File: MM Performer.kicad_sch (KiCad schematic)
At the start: 39 parts, among them IC1 MC68000P, U1 MC68030RC, U2 MC68881FN-SOC, U3 ATF16V8BJ, U4 ATF16V8BJ, U5 ATF16V8BJ, U6 ATF16V8BJ, U7 ATF16V8BJ

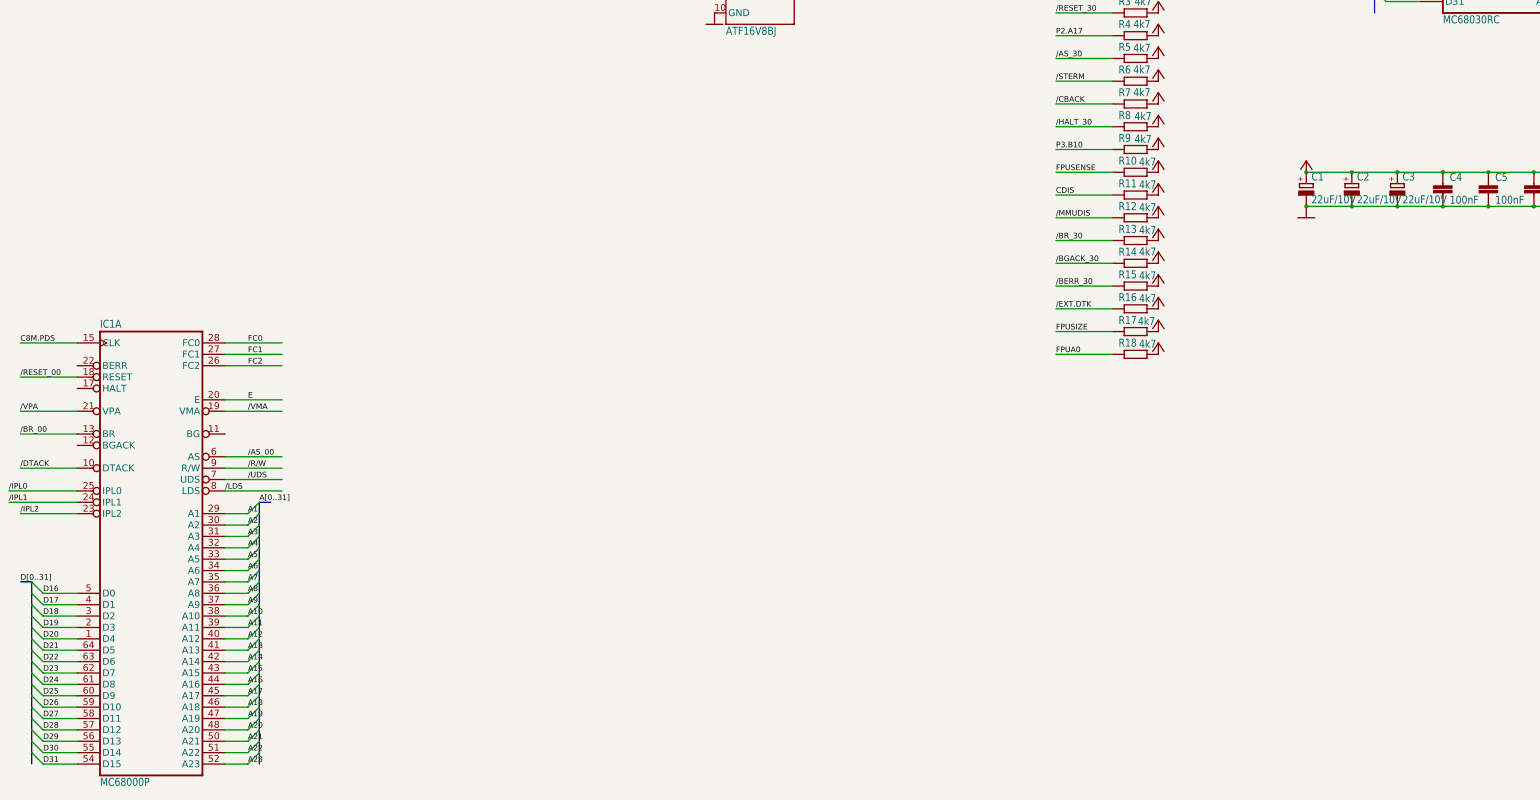
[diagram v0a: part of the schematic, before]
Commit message: Tweak positioning a bit
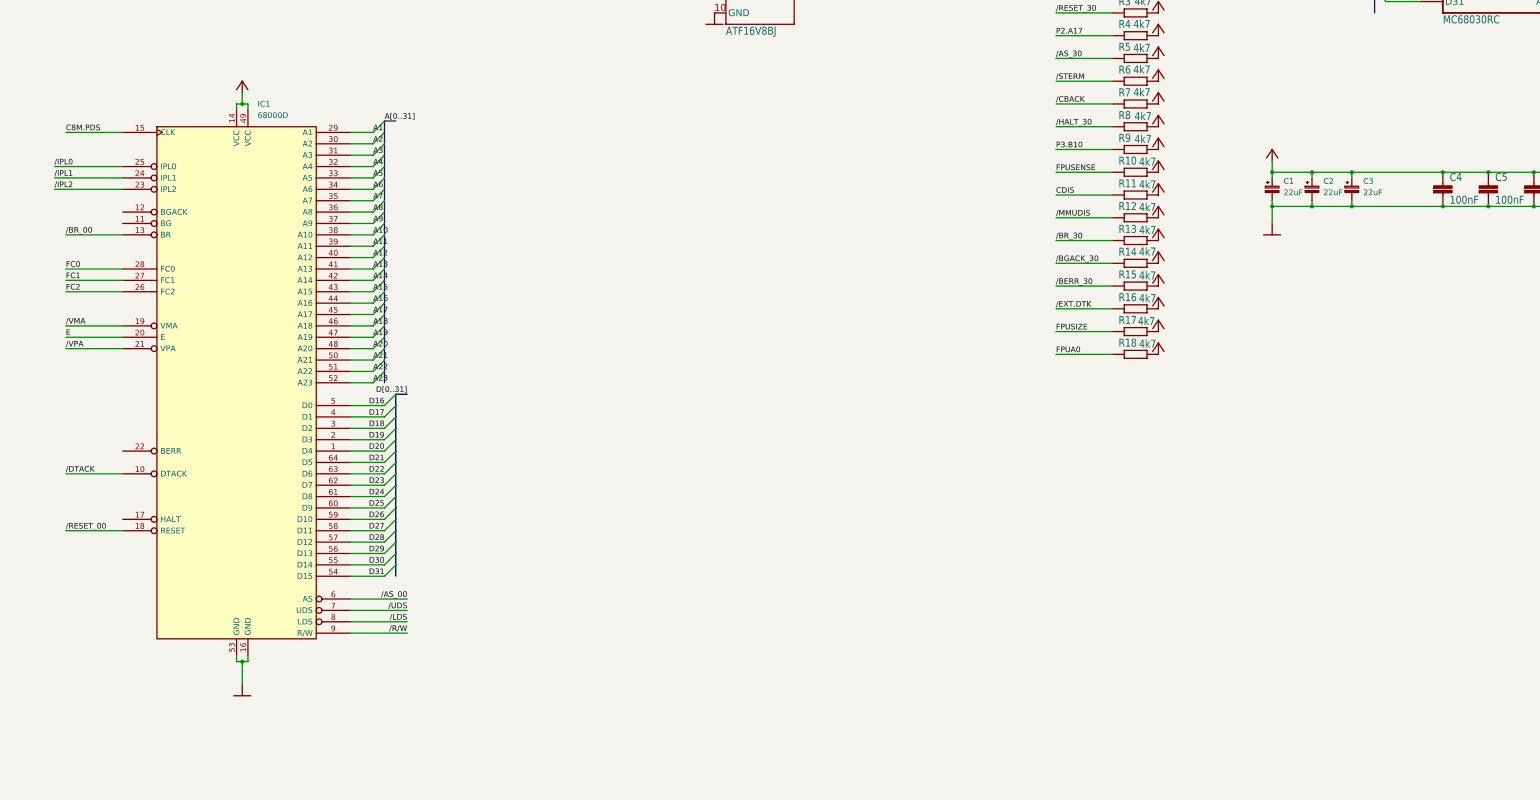
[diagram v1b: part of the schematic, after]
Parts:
- removed C1, C2, C3: 22uF/10V, Capacitor_Tantalum_SMD:CP_EIA-6032-28_Kemet-C_Pad2.25x2.35mm_HandSolder, symbol MM Performer-eagle-import:CPOL-EUC/6032-28W
- removed IC1: MC68000P, Package_DIP:DIP-64_W22.86mm, symbol MM Performer-eagle-import:MC68000P
- added C1, C2, C3: 22uF, Capacitor_Tantalum_SMD:CP_EIA-6032-28_Kemet-C_Pad2.25x2.35mm_HandSolder, symbol Device:C_Polarized_Small
- added IC1: 68000D, Package_DIP:DIP-64_W22.86mm, symbol CPU_NXP_68000:68000D
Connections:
- net /AS_00: now also IC1.6 (AS)
- net /BR_00: now also IC1.13 (BR)
- net /DTACK: now also IC1.10 (DTACK)
- net /IPL0: now also IC1.25 (IPL0)
- net /IPL1: now also IC1.24 (IPL1)
- net /IPL2: now also IC1.23 (IPL2)
- net /LDS: now also IC1.8 (LDS)
- net /R/W: now also IC1.9 (R/W)
- net /RESET_00: now also IC1.18 (RESET)
- net /UDS: now also IC1.7 (UDS)
- net /VMA: now also IC1.19 (VMA)
- net /VPA: now also IC1.21 (VPA)
- net A1: now also IC1.29 (A1)
- net A10: now also IC1.38 (A10)
- net A11: now also IC1.39 (A11)
- net A12: now also IC1.40 (A12)
- net A13: now also IC1.41 (A13)
- net A14: now also IC1.42 (A14)
- net A15: now also IC1.43 (A15)
- net A16: now also IC1.44 (A16)
- net A17: now also IC1.45 (A17)
- net A18: now also IC1.46 (A18)
- net A19: now also IC1.47 (A19)
- net A2: now also IC1.30 (A2)
- net A20: now also IC1.48 (A20)
- net A21: now also IC1.50 (A21)
- net A22: now also IC1.51 (A22)
- net A23: now also IC1.52 (A23)
- net A3: now also IC1.31 (A3)
- net A4: now also IC1.32 (A4)
- net A5: now also IC1.33 (A5)
- net A6: now also IC1.34 (A6)
- net A7: now also IC1.35 (A7)
- net A8: now also IC1.36 (A8)
- net A9: now also IC1.37 (A9)
- net C8M.PDS: now also IC1.15 (CLK)
- net D16: now also IC1.5 (D0)
- net D17: now also IC1.4 (D1)
- net D18: now also IC1.3 (D2)
- net D19: now also IC1.2 (D3)
- net D20: now also IC1.1 (D4)
- net D21: now also IC1.64 (D5)
- net D22: now also IC1.63 (D6)
- net D23: now also IC1.62 (D7)
- net D24: now also IC1.61 (D8)
- net D25: now also IC1.60 (D9)
- net D26: now also IC1.59 (D10)
- net D27: now also IC1.58 (D11)
- net D28: now also IC1.57 (D12)
- net D29: now also IC1.56 (D13)
- net D30: now also IC1.55 (D14)
- net D31: now also IC1.54 (D15)
- net E: now also IC1.20 (E)
- net FC0: now also IC1.28 (FC0)
- net FC1: now also IC1.27 (FC1)
- net FC2: now also IC1.26 (FC2)
- net GND: now also C1.2, C2.2, C3.2, IC1.16 (GND), IC1.53 (GND)
- net VCC: now also C1.1, C2.1, C3.1, IC1.14 (VCC), IC1.49 (VCC)

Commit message: Reorganize a bit
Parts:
- U3, U4, U5, U6: footprint Package_DIP:DIP-20_W7.62mm -> footprints:PLCC-20_THT-Socket
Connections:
- net GND: now also U1.C05 (GND@1), U1.C07 (GND@2), U1.C09 (GND@3), U1.E03 (GND@4), U1.E11 (GND@5), U1.F03 (GND@6), U1.G03 (GND@7), U1.G11 (GND@8), U1.J03 (GND@9), U1.J11 (GND@10), U1.L05 (GND@11), U1.L07 (GND@12), U1.L08 (GND@13), U1.L09 (GND@14), U2.12 (GND@6), U2.14 (GND@7), U2.19 (GND@8), U2.30 (GND@9), U2.41 (GND@10), U2.5 (GND@1), U2.51 (GND@11), U2.6 (GND@2), U2.63 (GND@12), U2.7 (GND@3), U2.8 (GND@4), U2.9 (GND@5)
- net VCC: now also U1.C06 (VCC@1), U1.D04 (VCC@2), U1.D10 (VCC@3), U1.F02 (VCC@4), U1.F11 (VCC@5), U1.H03 (VCC@6), U1.H11 (VCC@7), U1.K04 (VCC@8), U1.K10 (VCC@9), U1.L06 (VCC@10), U2.10 (VCC@1), U2.16 (VCC@2), U2.17 (VCC@3), U2.27 (VCC@4), U2.43 (VCC@5), U2.52 (VCC@6), U2.53 (VCC@7), U2.61 (VCC@8)

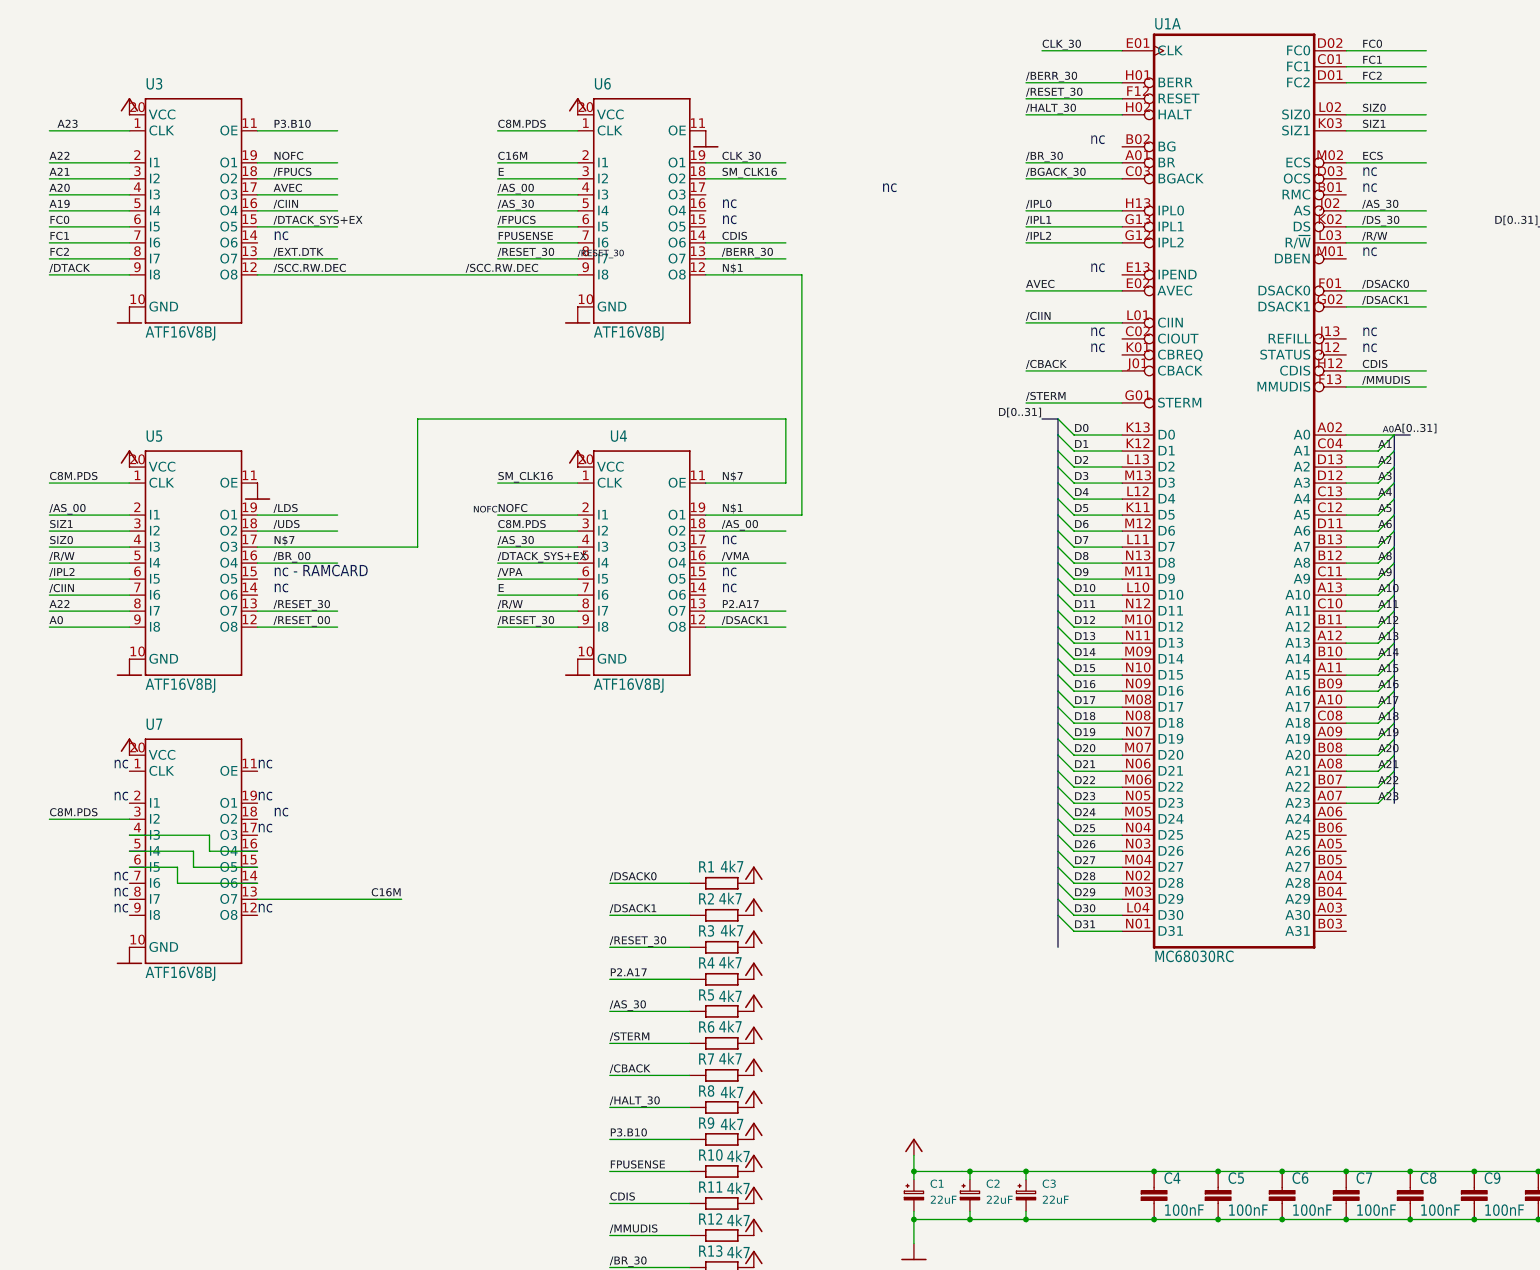
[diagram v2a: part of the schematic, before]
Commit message: Reorganize the positions
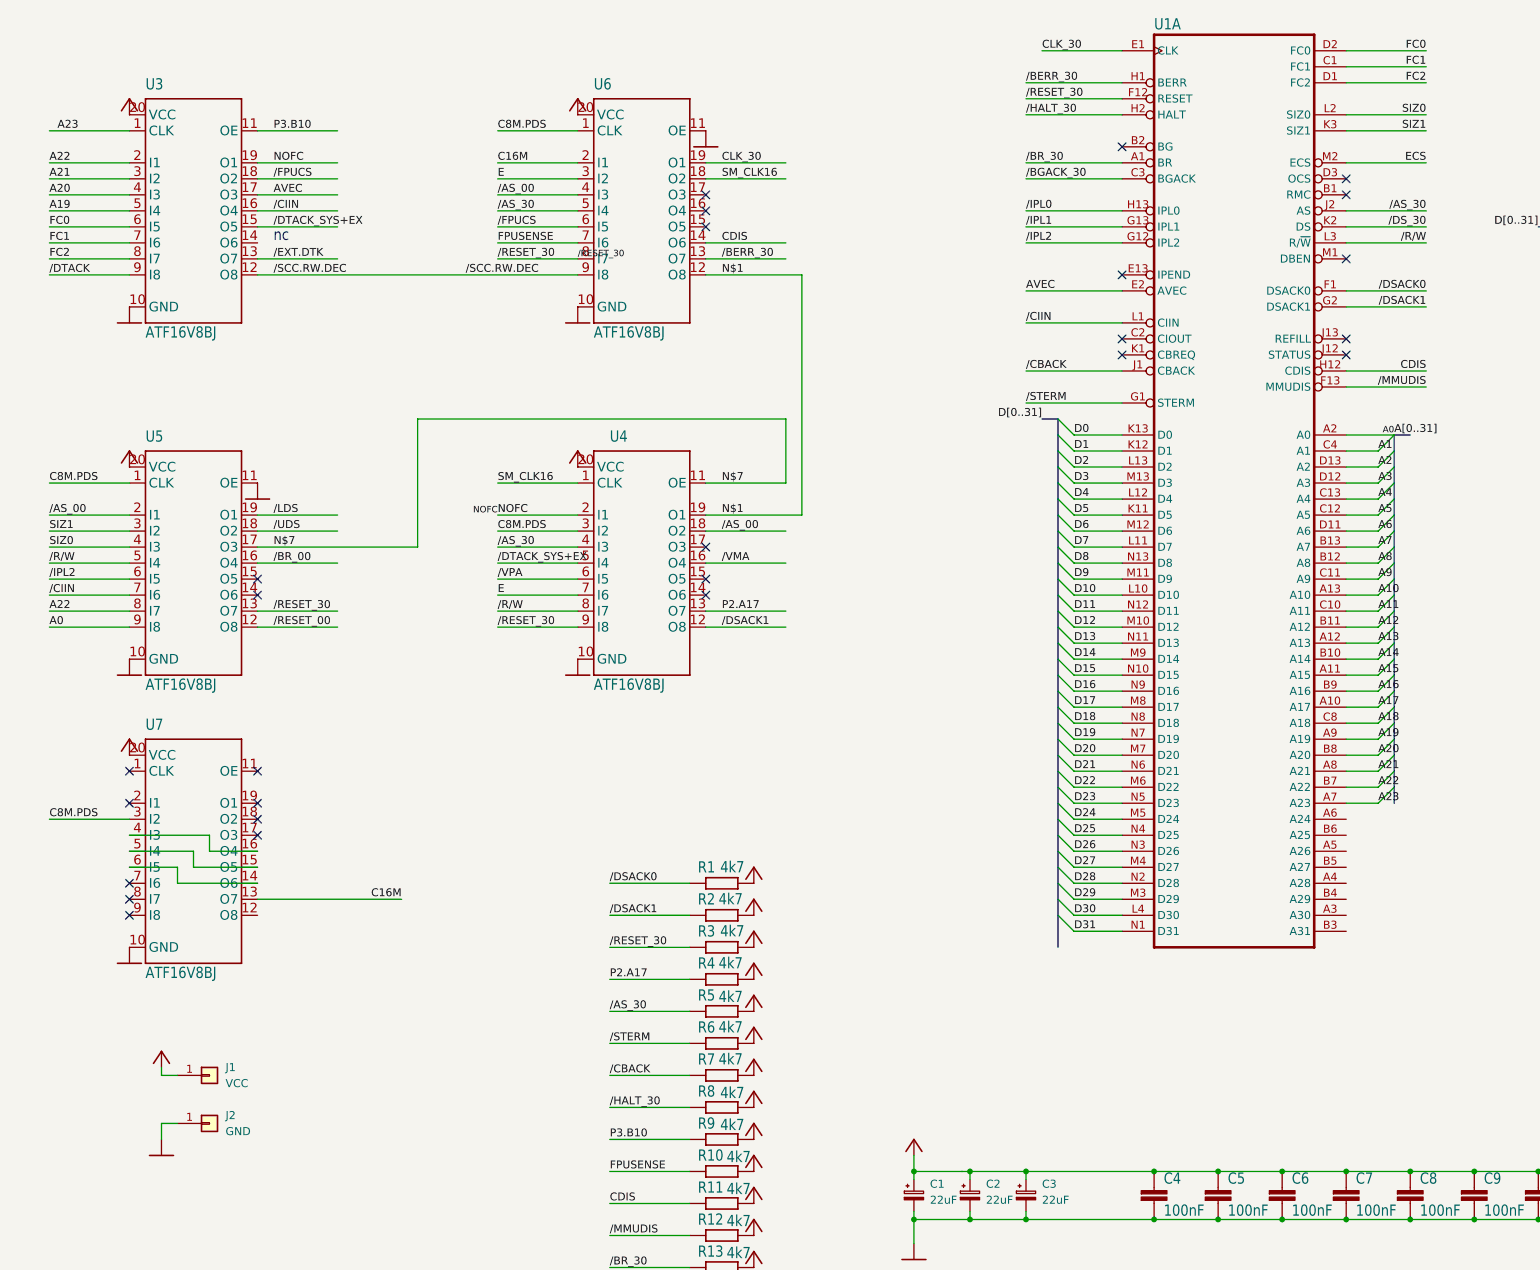
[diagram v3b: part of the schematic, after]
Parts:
- added J1: VCC, TestPoint:TestPoint_THTPad_4.0x4.0mm_Drill2.0mm, symbol Connector_Generic:Conn_01x01
- added J2: GND, TestPoint:TestPoint_THTPad_4.0x4.0mm_Drill2.0mm, symbol Connector_Generic:Conn_01x01
- added unit 1 of U1
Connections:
- net /AS_30: now also U1.J2 (AS); no longer U1.J02 (AS)
- net /BERR_30: now also U1.H1 (BERR); no longer U1.H01 (BERR)
- net /BGACK_30: now also U1.C3 (BGACK); no longer U1.C03 (BGACK)
- net /BR_30: now also U1.A1 (BR); no longer U1.A01 (BR)
- net /CBACK: now also U1.J1 (CBACK); no longer U1.J01 (CBACK)
- net /CIIN: now also U1.L1 (CIIN); no longer U1.L01 (CIIN)
- net /DSACK0: now also U1.F1 (DSACK0); no longer U1.F01 (DSACK0)
- net /DSACK1: now also U1.G2 (DSACK1); no longer U1.G02 (DSACK1)
- net /DS_30: now also U1.K2 (DS); no longer U1.K02 (DS)
- net /HALT_30: now also U1.H2 (HALT); no longer U1.H02 (HALT)
- net /IPL0: now also U1.H13 (IPL0); no longer U1.H13 (IPL0)
- net /IPL1: now also U1.G13 (IPL1); no longer U1.G13 (IPL1)
- net /IPL2: now also U1.G12 (IPL2); no longer U1.G12 (IPL2)
- net /MMUDIS: now also U1.F13 (MMUDIS); no longer U1.F13 (MMUDIS)
- net /R/W: now also U1.L3 (R/~{W}); no longer U1.L03 (R/~{W})
- net /RESET_30: now also U1.F12 (RESET); no longer U1.F12 (RESET)
- net /STERM: now also U1.G1 (STERM); no longer U1.G01 (STERM)
- net A0: now also U1.A2 (A0); no longer U1.A02 (A0)
- net A1: now also U1.C4 (A1); no longer U1.C04 (A1)
- net A10: now also U1.A13 (A10); no longer U1.A13 (A10)
- net A11: now also U1.C10 (A11); no longer U1.C10 (A11)
- net A12: now also U1.B11 (A12); no longer U1.B11 (A12)
- net A13: now also U1.A12 (A13); no longer U1.A12 (A13)
- net A14: now also U1.B10 (A14); no longer U1.B10 (A14)
- net A15: now also U1.A11 (A15); no longer U1.A11 (A15)
- net A16: now also U1.B9 (A16); no longer U1.B09 (A16)
- net A17: now also U1.A10 (A17); no longer U1.A10 (A17)
- net A18: now also U1.C8 (A18); no longer U1.C08 (A18)
- net A19: now also U1.A9 (A19); no longer U1.A09 (A19)
- net A2: now also U1.D13 (A2); no longer U1.D13 (A2)
- net A20: now also U1.B8 (A20); no longer U1.B08 (A20)
- net A21: now also U1.A8 (A21); no longer U1.A08 (A21)
- net A22: now also U1.B7 (A22); no longer U1.B07 (A22)
- net A23: now also U1.A7 (A23); no longer U1.A07 (A23)
- net A3: now also U1.D12 (A3); no longer U1.D12 (A3)
- net A4: now also U1.C13 (A4); no longer U1.C13 (A4)
- net A5: now also U1.C12 (A5); no longer U1.C12 (A5)
- net A6: now also U1.D11 (A6); no longer U1.D11 (A6)
- net A7: now also U1.B13 (A7); no longer U1.B13 (A7)
- net A8: now also U1.B12 (A8); no longer U1.B12 (A8)
- net A9: now also U1.C11 (A9); no longer U1.C11 (A9)
- net AVEC: now also U1.E2 (AVEC); no longer U1.E02 (AVEC)
- net CDIS: now also U1.H12 (CDIS); no longer U1.H12 (CDIS)
- net CLK_30: now also U1.E1 (CLK); no longer U1.E01 (CLK)
- net D0: now also U1.K13 (D0); no longer U1.K13 (D0)
- net D1: now also U1.K12 (D1); no longer U1.K12 (D1)
- net D10: now also U1.L10 (D10); no longer U1.L10 (D10)
- net D11: now also U1.N12 (D11); no longer U1.N12 (D11)
- net D12: now also U1.M10 (D12); no longer U1.M10 (D12)
- net D13: now also U1.N11 (D13); no longer U1.N11 (D13)
- net D14: now also U1.M9 (D14); no longer U1.M09 (D14)
- net D15: now also U1.N10 (D15); no longer U1.N10 (D15)
- net D16: now also U1.N9 (D16); no longer U1.N09 (D16)
- net D17: now also U1.M8 (D17); no longer U1.M08 (D17)
- net D18: now also U1.N8 (D18); no longer U1.N08 (D18)
- net D19: now also U1.N7 (D19); no longer U1.N07 (D19)
- net D2: now also U1.L13 (D2); no longer U1.L13 (D2)
- net D20: now also U1.M7 (D20); no longer U1.M07 (D20)
- net D21: now also U1.N6 (D21); no longer U1.N06 (D21)
- net D22: now also U1.M6 (D22); no longer U1.M06 (D22)
- net D23: now also U1.N5 (D23); no longer U1.N05 (D23)
- net D24: now also U1.M5 (D24); no longer U1.M05 (D24)
- net D25: now also U1.N4 (D25); no longer U1.N04 (D25)
- net D26: now also U1.N3 (D26); no longer U1.N03 (D26)
- net D27: now also U1.M4 (D27); no longer U1.M04 (D27)
- net D28: now also U1.N2 (D28); no longer U1.N02 (D28)
- net D29: now also U1.M3 (D29); no longer U1.M03 (D29)
- net D3: now also U1.M13 (D3); no longer U1.M13 (D3)
- net D30: now also U1.L4 (D30); no longer U1.L04 (D30)
- net D31: now also U1.N1 (D31); no longer U1.N01 (D31)
- net D4: now also U1.L12 (D4); no longer U1.L12 (D4)
- net D5: now also U1.K11 (D5); no longer U1.K11 (D5)
- net D6: now also U1.M12 (D6); no longer U1.M12 (D6)
- net D7: now also U1.L11 (D7); no longer U1.L11 (D7)
- net D8: now also U1.N13 (D8); no longer U1.N13 (D8)
- net D9: now also U1.M11 (D9); no longer U1.M11 (D9)
- net ECS: now also U1.M2 (ECS); no longer U1.M02 (ECS)
- net FC0: now also U1.D2 (FC0); no longer U1.D02 (FC0)
- net FC1: now also U1.C1 (FC1); no longer U1.C01 (FC1)
- net FC2: now also U1.D1 (FC2); no longer U1.D01 (FC2)
- net GND: now also J2.1 (Pin_1)
- net SIZ0: now also U1.L2 (SIZ0); no longer U1.L02 (SIZ0)
- net SIZ1: now also U1.K3 (SIZ1); no longer U1.K03 (SIZ1)
- net VCC: now also J1.1 (Pin_1)
- new net: U1.D5 (NC), U1.E12 (NC), U1.F10 (NC), U1.F4 (NC), U1.K5 (NC)
- no-connect marks 0 -> 26
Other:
- note removed: "nc - RAMCARD"

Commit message: Performer
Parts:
- added unit 2 of U2
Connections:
- net GND: now also U2.12 (GND@6), U2.14 (GND@7), U2.19 (GND@8), U2.30 (GND@9), U2.41 (GND@10), U2.5 (GND@1), U2.51 (GND@11), U2.6 (GND@2), U2.63 (GND@12), U2.7 (GND@3), U2.8 (GND@4), U2.9 (GND@5); no longer U2.12 (GND@6), U2.14 (GND@7), U2.19 (GND@8), U2.30 (GND@9), U2.41 (GND@10), U2.5 (GND@1), U2.51 (GND@11), U2.6 (GND@2), U2.63 (GND@12), U2.7 (GND@3), U2.8 (GND@4), U2.9 (GND@5)
- net VCC: now also U2.10 (VCC@1), U2.16 (VCC@2), U2.17 (VCC@3), U2.27 (VCC@4), U2.43 (VCC@5), U2.52 (VCC@6), U2.53 (VCC@7), U2.61 (VCC@8); no longer U2.10 (VCC@1), U2.16 (VCC@2), U2.17 (VCC@3), U2.27 (VCC@4), U2.43 (VCC@5), U2.52 (VCC@6), U2.53 (VCC@7), U2.61 (VCC@8)
- no-connect marks 26 -> 30
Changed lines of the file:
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@@
+	)
+	(no_connect
+		(at 53.34 273.05)
 	)
 	(no_connect
@@
 	)
 	(no_connect
+		(at 53.34 288.29)
+	)
+	(no_connect
 		(at 205.74 147.32)
 	)
 	(no_connect
 		(at 185.42 167.64)
+	)
+	(no_connect
+		(at 53.34 222.25)
 	)
 	(no_connect
@@
 	)
 	(no_connect
+		(at 53.34 219.71)
+	)
+	(no_connect
